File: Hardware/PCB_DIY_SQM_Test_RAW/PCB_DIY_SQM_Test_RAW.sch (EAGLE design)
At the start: 10 parts, among them U1 MLX90614_, U2 ARDUINO_SHIELDLONGPADS

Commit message: The DS18B20 now connects to Arduino pin #10 instead of pin #11. This allows us to use the Wireless SD shield (which uses pin #11 for SPI)
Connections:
- net DS18B20P2: now also U2.*D10; no longer U2.*D11
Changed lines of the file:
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@@
 <wire x1="116.84" y1="50.8" x2="116.84" y2="48.26" width="0.1524" layer="91"/>
 <pinref part="R3" gate="G$1" pin="1"/>
-</segment>
-<segment>
-<pinref part="U2" gate="G$1" pin="*D11"/>
-<wire x1="86.36" y1="5.08" x2="106.68" y2="5.08" width="0.1524" layer="91"/>
+<pinref part="U2" gate="G$1" pin="*D10"/>
+<wire x1="86.36" y1="7.62" x2="106.68" y2="7.62" width="0.1524" layer="91"/>
+<wire x1="106.68" y1="7.62" x2="106.68" y2="48.26" width="0.1524" layer="91"/>
+<wire x1="106.68" y1="48.26" x2="116.84" y2="48.26" width="0.1524" layer="91"/>
+<junction x="116.84" y="48.26"/>
 </segment>
 </net>

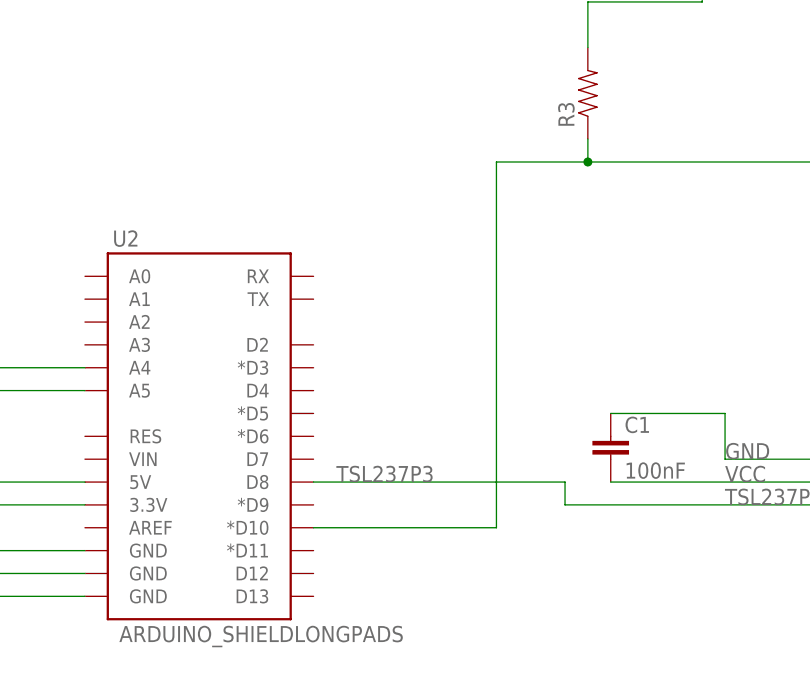
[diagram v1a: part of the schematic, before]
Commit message: DS18B20 now uses Arduino pin #9 instead of #10, because #10 is used by the SD card of the wireless SD shield. Added support for SD cards. The sketch writes the data to a file called test.txt on the sd card (if available)
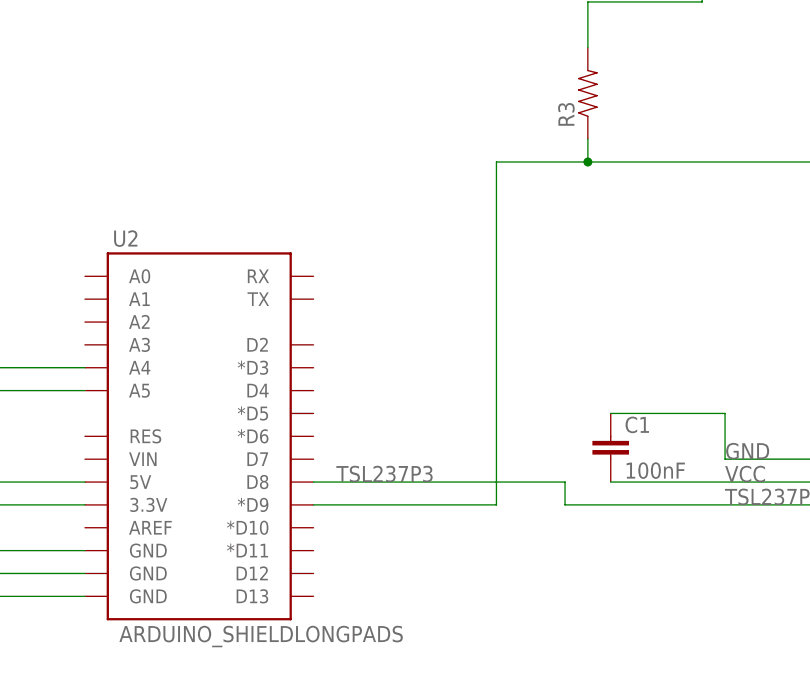
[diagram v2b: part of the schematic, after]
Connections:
- net DS18B20P2: now also U2.*D9; no longer U2.*D10
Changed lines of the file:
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@@
 <wire x1="116.84" y1="50.8" x2="116.84" y2="48.26" width="0.1524" layer="91"/>
 <pinref part="R3" gate="G$1" pin="1"/>
-<pinref part="U2" gate="G$1" pin="*D10"/>
-<wire x1="86.36" y1="7.62" x2="106.68" y2="7.62" width="0.1524" layer="91"/>
-<wire x1="106.68" y1="7.62" x2="106.68" y2="48.26" width="0.1524" layer="91"/>
 <wire x1="106.68" y1="48.26" x2="116.84" y2="48.26" width="0.1524" layer="91"/>
 <junction x="116.84" y="48.26"/>
+<pinref part="U2" gate="G$1" pin="*D9"/>
+<wire x1="86.36" y1="10.16" x2="106.68" y2="10.16" width="0.1524" layer="91"/>
+<wire x1="106.68" y1="10.16" x2="106.68" y2="48.26" width="0.1524" layer="91"/>
 </segment>
 </net>

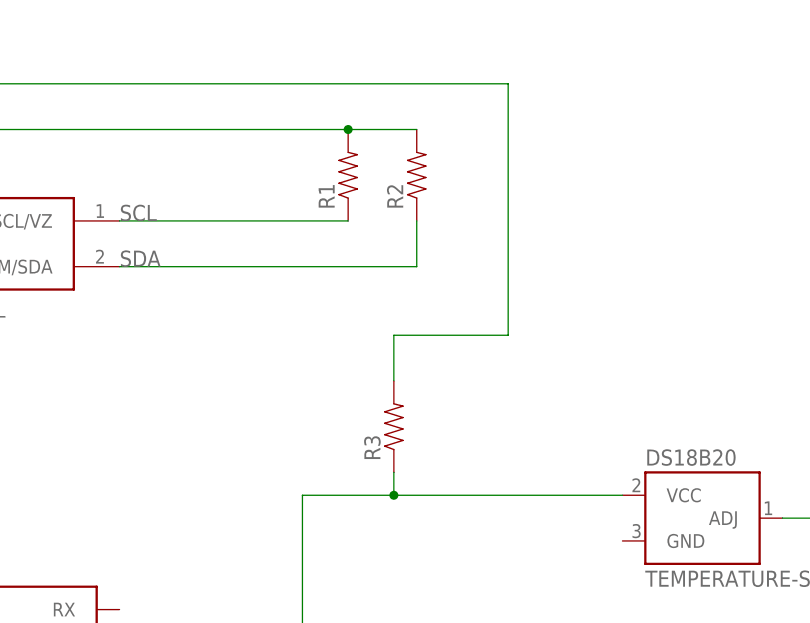
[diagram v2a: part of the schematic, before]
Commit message: all resitsors are 4.7 kilo ohms.
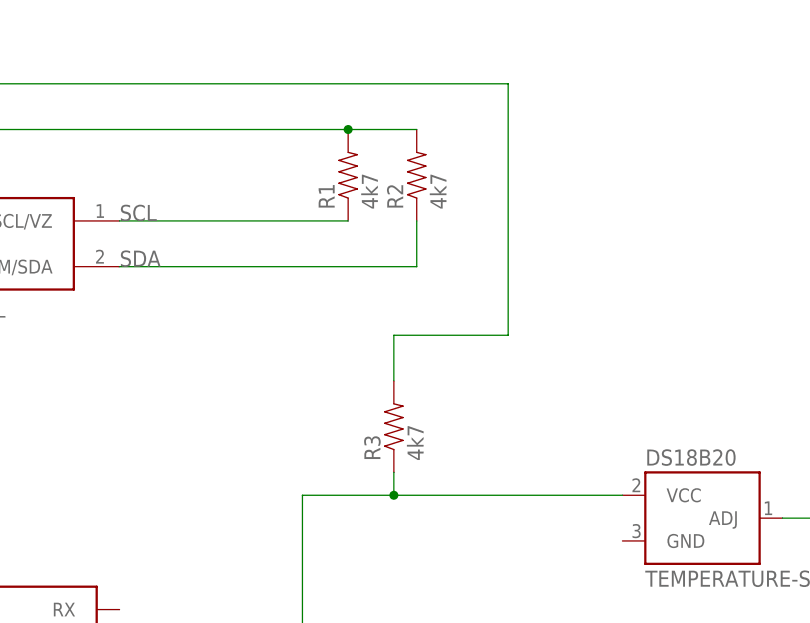
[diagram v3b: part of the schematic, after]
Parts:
- R1, R2, R3: value (none) -> 4k7
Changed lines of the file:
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@@
 <part name="TSL237" library="SparkFun-Connectors" deviceset="M03" device="LOCK_LONGPADS"/>
 <part name="U$3" library="SparkFun-Aesthetics" deviceset="5V" device=""/>
-<part name="R1" library="SparkFun-Passives" deviceset="RESISTOR" device="PTH-1/4W"/>
-<part name="R2" library="SparkFun-Passives" deviceset="RESISTOR" device="PTH-1/4W"/>
-<part name="R3" library="SparkFun-Passives" deviceset="RESISTOR" device="PTH-1/4W"/>
+<part name="R1" library="SparkFun-Passives" deviceset="RESISTOR" device="PTH-1/4W" value="4k7"/>
+<part name="R2" library="SparkFun-Passives" deviceset="RESISTOR" device="PTH-1/4W" value="4k7"/>
+<part name="R3" library="SparkFun-Passives" deviceset="RESISTOR" device="PTH-1/4W" value="4k7"/>
 <part name="C1" library="SparkFun-Passives" deviceset="CAP" device="PTH" value="100nF"/>
 <part name="C3" library="SparkFun-Passives" deviceset="CAP" device="PTH" value="100nF"/>
